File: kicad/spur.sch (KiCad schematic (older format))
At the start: 35 parts, among them J1 USB_A, SW1 JS102000SAQN, U1 MIC5377YC5, U2 AT25SF081-MAHB-X, U3 STM32F401CBUx, Y1 24MHz

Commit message: Remove UART test points
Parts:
- removed TP5: TXO, TestPoint:TestPoint_Pad_D1.0mm, symbol Connector:TestPoint
- removed TP6: RXI, TestPoint:TestPoint_Pad_D1.0mm, symbol Connector:TestPoint
- renumbered TP7 to TP5, TP8 to TP6
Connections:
- net UART_RXI: no longer names the net of U3.13 (PA3)
- net UART_TXO: no longer names the net of U3.12 (PA2)
- no-connect marks 23 -> 25
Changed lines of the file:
@@
 Sheet 1 1
 Title "Spur - A physical UEFI boot switch"
-Date "2020-09-20"
+Date "2020-09-22"
 Rev "v1.0"
 Comp "Ian Glen <ian@ianglen.me>"
@@
 	1    0    0    -1
 $EndComp
-Text Label 9800 4700 2    50   ~ 0
-UART_TXO
-Text Label 9800 4800 2    50   ~ 0
-UART_RXI
 Text Label 9800 5000 2    50   ~ 0
 SPI_SCK
@@
 Connection ~ 7000 3400
 $Comp
-L Connector:TestPoint TP7
+L Connector:TestPoint TP5
 U 1 1 5F6B941A
 P 9850 5800
-F 0 "TP7" V 9850 6050 50  0000 C CNN
+F 0 "TP5" V 9850 6050 50  0000 C CNN
 F 1 "SWDIO" V 9954 5872 50  0001 C CNN
 F 2 "TestPoint:TestPoint_Pad_D1.0mm" H 10050 5800 50  0001 C CNN
@@
 $EndComp
 $Comp
-L Connector:TestPoint TP8
+L Connector:TestPoint TP6
 U 1 1 5F6B9F42
 P 9850 5900
-F 0 "TP8" V 9850 6150 50  0000 C CNN
+F 0 "TP6" V 9850 6150 50  0000 C CNN
 F 1 "SWCLK" V 9954 5972 50  0001 C CNN
 F 2 "TestPoint:TestPoint_Pad_D1.0mm" H 10050 5900 50  0001 C CNN
@@
 Wire Wire Line
 	9350 5900 9850 5900
-$Comp
-L Connector:TestPoint TP5
-U 1 1 5F6C581E
-P 9850 4700
-F 0 "TP5" V 9850 4950 50  0000 C CNN
-F 1 "TXO" V 9954 4772 50  0001 C CNN
-F 2 "TestPoint:TestPoint_Pad_D1.0mm" H 10050 4700 50  0001 C CNN
-F 3 "~" H 10050 4700 50  0001 C CNN
-	1    9850 4700
-	0    1    1    0
-$EndComp
-$Comp
-L Connector:TestPoint TP6
-U 1 1 5F6C5828
-P 9850 4800
-F 0 "TP6" V 9850 5050 50  0000 C CNN
-F 1 "RXI" V 9954 4872 50  0001 C CNN
-F 2 "TestPoint:TestPoint_Pad_D1.0mm" H 10050 4800 50  0001 C CNN
-F 3 "~" H 10050 4800 50  0001 C CNN
-	1    9850 4800
-	0    1    1    0
-$EndComp
-Wire Wire Line
-	9350 4700 9850 4700
-Wire Wire Line
-	9350 4800 9850 4800
 $Comp
 L Connector:TestPoint TP2
@@
 Wire Wire Line
 	7500 4700 8050 4700
+NoConn ~ 9350 4700
+NoConn ~ 9350 4800
 $EndSCHEMATC

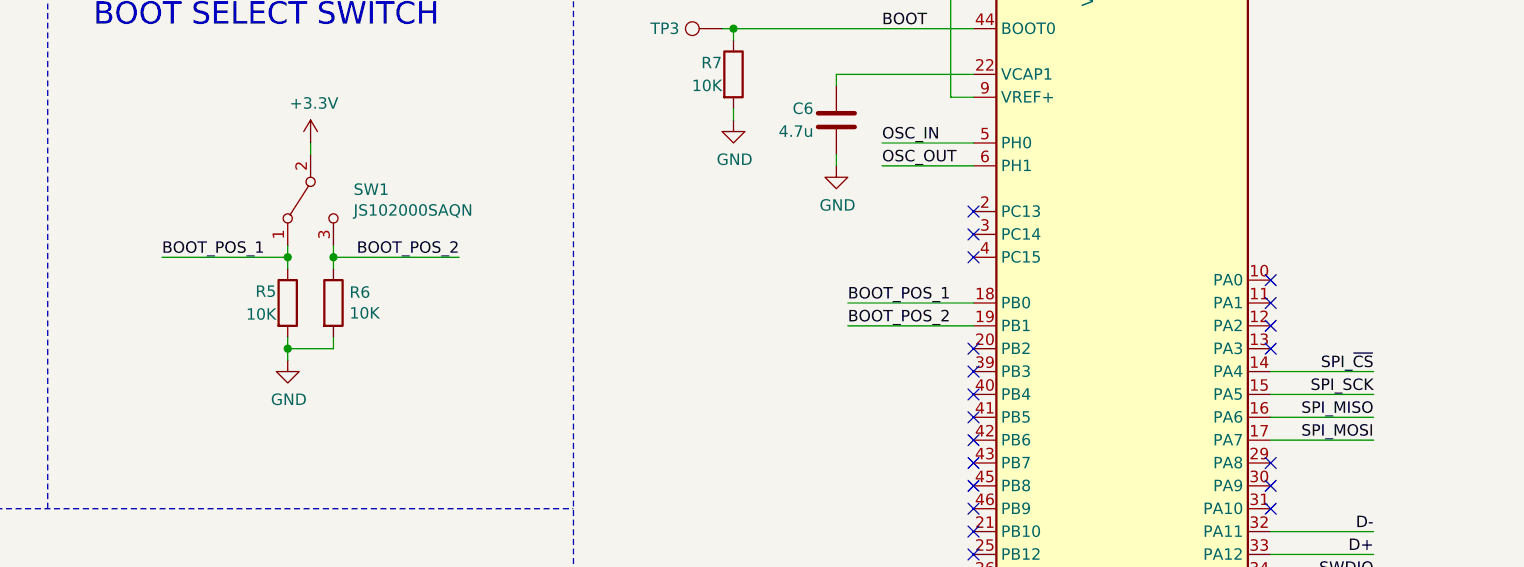
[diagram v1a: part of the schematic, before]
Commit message: Move switch input pins
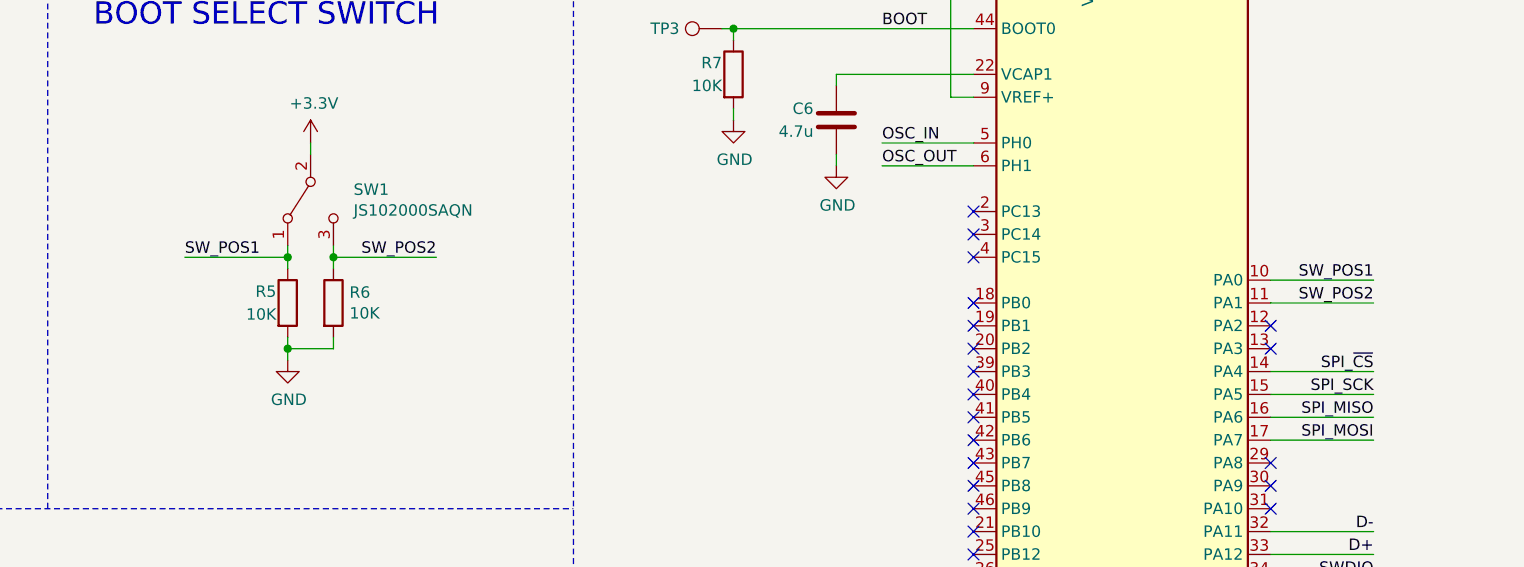
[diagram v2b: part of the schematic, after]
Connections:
- net SW_POS1: now reaches U3.10 (PA0)
- net SW_POS1: now also R5.1, SW1.1 (A)
- net SW_POS2: now reaches U3.11 (PA1)
- net SW_POS2: now also R6.1, SW1.3 (C)
- removed net BOOT_POS_1: R5.1, SW1.1 (A), U3.18 (PB0)
- removed net BOOT_POS_2: R6.1, SW1.3 (C), U3.19 (PB1)
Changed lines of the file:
@@
 Wire Wire Line
 	5050 4800 5050 4750
-Text Label 4500 4400 0    50   ~ 0
-BOOT_POS_1
-Text Label 5800 4400 2    50   ~ 0
-BOOT_POS_2
-Wire Wire Line
-	5800 4400 5250 4400
+Wire Wire Line
+	5700 4400 5250 4400
 Connection ~ 5250 4400
 Wire Wire Line
 	5250 4400 5250 4350
 Wire Wire Line
-	5050 4400 4500 4400
+	5050 4400 4600 4400
 Connection ~ 5050 4400
 Wire Wire Line
@@
 NoConn ~ 9350 5400
 NoConn ~ 9350 5300
-NoConn ~ 9350 4600
-NoConn ~ 9350 4500
 NoConn ~ 8050 6000
 NoConn ~ 8050 5900
@@
 Wire Wire Line
 	3200 4000 3150 4000
-Text Label 7500 4600 0    50   ~ 0
-BOOT_POS_1
-Text Label 7500 4700 0    50   ~ 0
-BOOT_POS_2
-Wire Wire Line
-	8050 4600 7500 4600
-Wire Wire Line
-	7500 4700 8050 4700
+Text Label 9800 4600 2    50   ~ 0
+SW_POS2
+Text Label 9800 4500 2    50   ~ 0
+SW_POS1
+Wire Wire Line
+	9350 4600 9800 4600
+Wire Wire Line
+	9800 4500 9350 4500
 NoConn ~ 9350 4700
 NoConn ~ 9350 4800
+NoConn ~ 8050 4700
+NoConn ~ 8050 4600
+Text Label 4600 4400 0    50   ~ 0
+SW_POS1
+Text Label 5700 4400 2    50   ~ 0
+SW_POS2
 $EndSCHEMATC

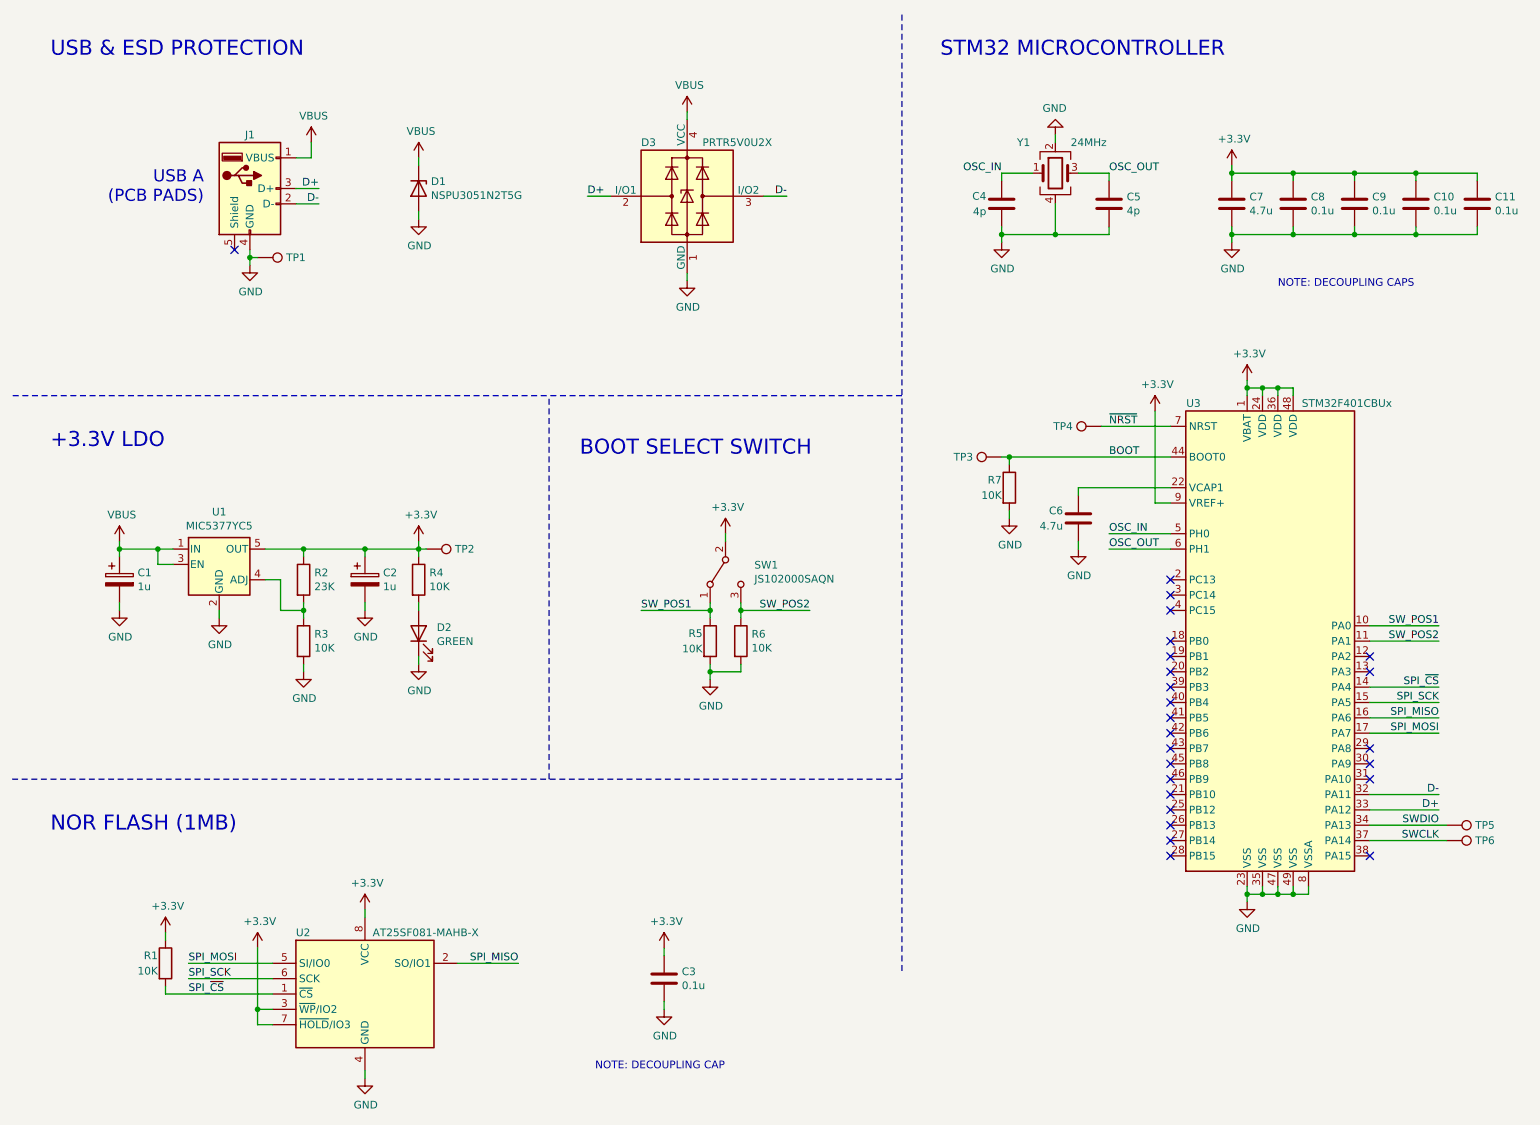
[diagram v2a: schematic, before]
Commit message: Update R2 value, fix C1 & C2 symbols, improve schematic notes
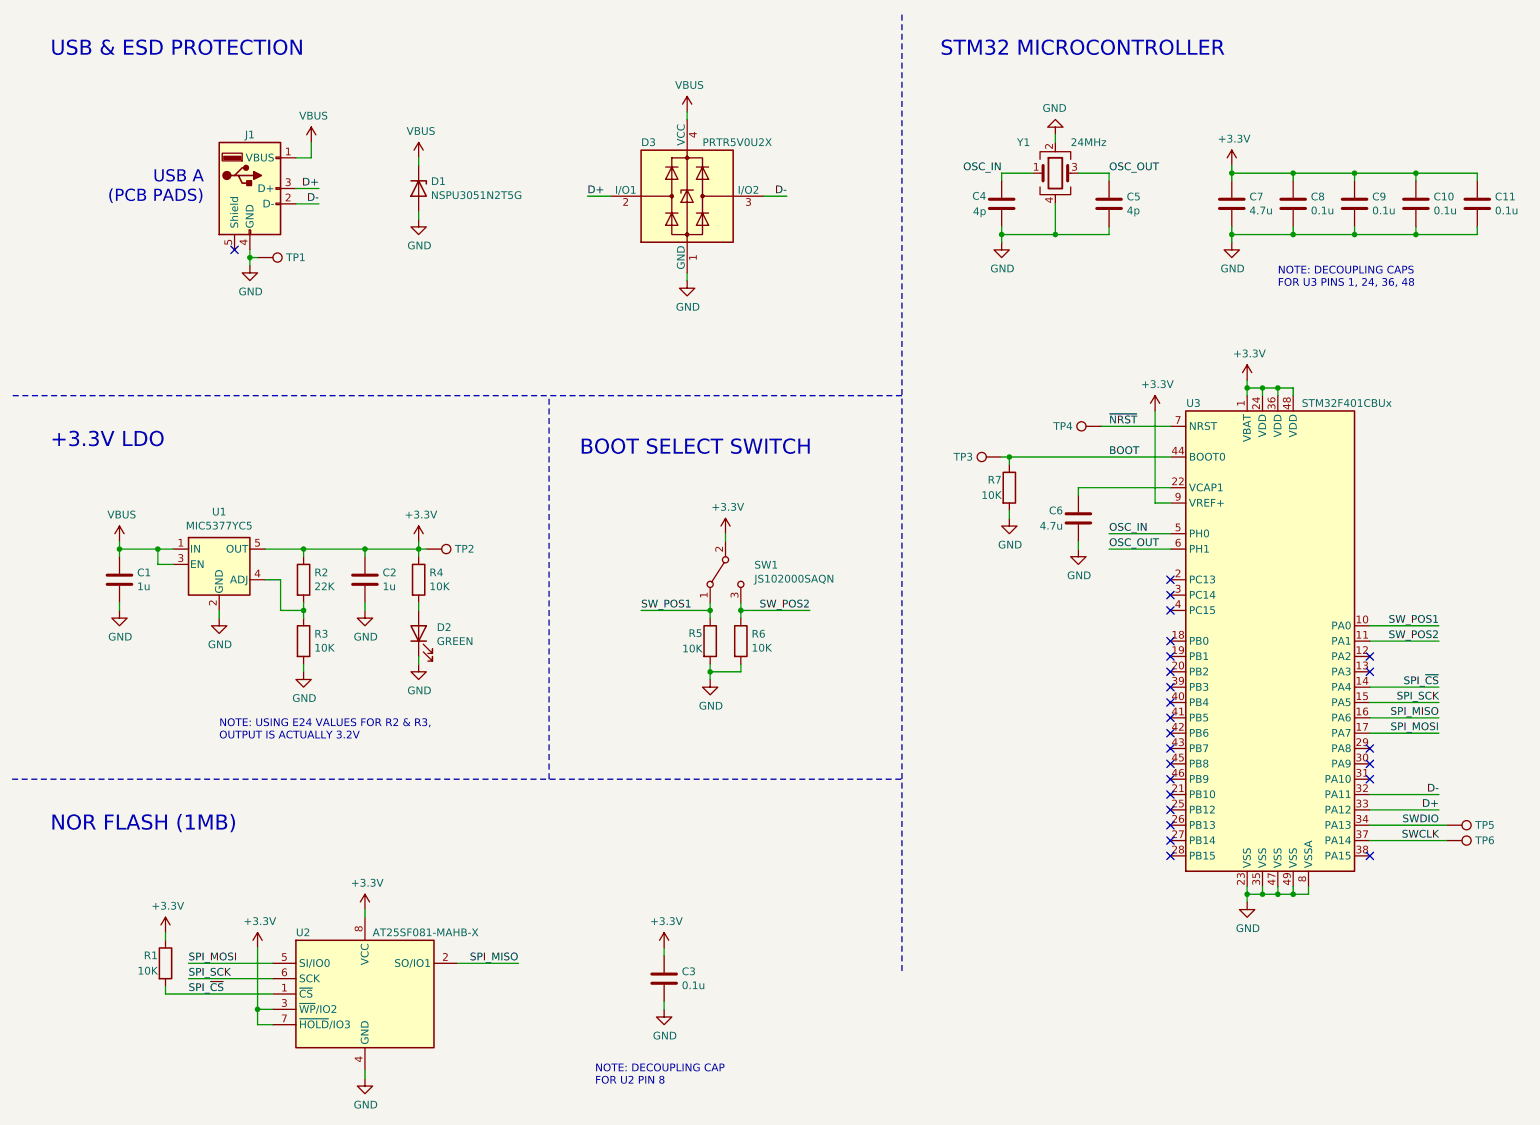
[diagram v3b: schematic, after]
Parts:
- removed C1, C2: 1u, Capacitor_SMD:C_0402_1005Metric, symbol Device:CP
- added C1, C2: 1u, Capacitor_SMD:C_0402_1005Metric, symbol Device:C
- R2: value 23K -> 22K
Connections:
- net +3V3: now also C2.1
- net GND: now also C1.2, C2.2
- net VBUS: now also C1.1
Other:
- note added: "NOTE: DECOUPLING CAPS\nFOR U3 PINS 1, 24, 36, 48"
- note added: "NOTE: DECOUPLING CAP\nFOR U2 PIN 8"
- note added: "NOTE: USING E24 VALUES FOR R2 & R3,\nOUTPUT IS ACTUALLY 3.2V"
- note removed: "NOTE: DECOUPLING CAP"
- note removed: "NOTE: DECOUPLING CAPS"
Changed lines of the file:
@@
 Sheet 1 1
 Title "Spur - A physical UEFI boot switch"
-Date "2020-09-22"
+Date "2020-09-25"
 Rev "v1.0"
 Comp "Ian Glen <ian@ianglen.me>"
@@
 	500  5500 6300 5500
 $Comp
-L Device:CP C1
-U 1 1 5F69995A
-P 1200 4200
-F 0 "C1" H 1318 4246 50  0000 L CNN
-F 1 "1u" H 1318 4155 50  0000 L CNN
-F 2 "Capacitor_SMD:C_0402_1005Metric" H 1238 4050 50  0001 C CNN
-F 3 "~" H 1200 4200 50  0001 C CNN
-	1    1200 4200
-	1    0    0    -1
-$EndComp
-$Comp
 L power:GND #PWR0111
 U 1 1 5F69A270
@@
 	1550 4000 1450 4000
 $Comp
-L Device:CP C2
-U 1 1 5F69D2F8
-P 2800 4200
-F 0 "C2" H 2918 4246 50  0000 L CNN
-F 1 "1u" H 2918 4155 50  0000 L CNN
-F 2 "Capacitor_SMD:C_0402_1005Metric" H 2838 4050 50  0001 C CNN
-F 3 "~" H 2800 4200 50  0001 C CNN
-	1    2800 4200
-	1    0    0    -1
-$EndComp
-$Comp
 L power:GND #PWR0112
 U 1 1 5F69D302
@@
 P 2400 4200
 F 0 "R2" H 2470 4246 50  0000 L CNN
-F 1 "23K" H 2470 4155 50  0000 L CNN
+F 1 "22K" H 2470 4155 50  0000 L CNN
 F 2 "Resistor_SMD:R_0402_1005Metric" V 2330 4200 50  0001 C CNN
 F 3 "~" H 2400 4200 50  0001 C CNN
@@
 Text Label 7650 3200 0    50   ~ 0
 ~NRST
-Text Notes 4300 7400 0    50   ~ 0
-NOTE: DECOUPLING CAP
+Text Notes 4300 7500 0    50   ~ 0
+NOTE: DECOUPLING CAP\nFOR U2 PIN 8
 Wire Wire Line
 	7950 3100 7950 3700
@@
 	9800 4900 9350 4900
 Text Notes 8750 2300 0    50   ~ 0
-NOTE: DECOUPLING CAPS
+NOTE: DECOUPLING CAPS\nFOR U3 PINS 1, 24, 36, 48
 $Comp
 L power:+3.3V #PWR0130
@@
 Text Label 5700 4400 2    50   ~ 0
 SW_POS2
+Text Notes 1850 5250 0    50   ~ 0
+NOTE: USING E24 VALUES FOR R2 & R3,\nOUTPUT IS ACTUALLY 3.2V
+$Comp
+L Device:C C1
+U 1 1 5F6F755F
+P 1200 4200
+F 0 "C1" H 1315 4246 50  0000 L CNN
+F 1 "1u" H 1315 4155 50  0000 L CNN
+F 2 "Capacitor_SMD:C_0402_1005Metric" H 1238 4050 50  0001 C CNN
+F 3 "~" H 1200 4200 50  0001 C CNN
+	1    1200 4200
+	1    0    0    -1
+$EndComp
+$Comp
+L Device:C C2
+U 1 1 5F6F9410
+P 2800 4200
+F 0 "C2" H 2915 4246 50  0000 L CNN
+F 1 "1u" H 2915 4155 50  0000 L CNN
+F 2 "Capacitor_SMD:C_0402_1005Metric" H 2838 4050 50  0001 C CNN
+F 3 "~" H 2800 4200 50  0001 C CNN
+	1    2800 4200
+	1    0    0    -1
+$EndComp
 $EndSCHEMATC

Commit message: Switch to internal pull-ups, remove 4.7uF bulk cap
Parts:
- removed C7: 4.7u, Capacitor_SMD:C_0402_1005Metric, symbol Device:C
- removed D2: GREEN, LED_SMD:LED_0402_1005Metric, symbol Device:LED
- removed R1, R4, R5, R6: 10K, Resistor_SMD:R_0402_1005Metric, symbol Device:R
- renumbered C11 to C10, C8 to C7, C9 to C8, C10 to C9, D3 to D2, R2 to R1, R3 to R2, R7 to R3
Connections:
- net +3V3: no longer SW1.2 (B)
- net GND: now also SW1.2 (B)
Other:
- note added: "NOTE: ENABLE INTERNAL PULL-UPS\nON SW_POS1, SW_POS2, AND SPI_~CS"
- moved on the sheet: C1, C10, C2, C7, C8, C9, R1, R2, SW1, TP2, U1

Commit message: Add custom footprint for flash chip
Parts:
- U2: footprint Package_SON:SON-8-1EP_3x2mm_P0.5mm_EP1.4x1.6mm -> spur:SON-8-1EP_3x2mm_P0.5mm_EP0.2x1.6mm
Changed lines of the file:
@@
 F 0 "U2" H 2350 7300 50  0000 L CNN
 F 1 "AT25SF081-MAHB-X" H 2850 7300 50  0000 L CNN
-F 2 "Package_SON:SON-8-1EP_3x2mm_P0.5mm_EP1.4x1.6mm" H 2800 6300 50  0001 C CNN
+F 2 "spur:SON-8-1EP_3x2mm_P0.5mm_EP0.2x1.6mm" H 2800 6300 50  0001 C CNN
 F 3 "https://www.adestotech.com/wp-content/uploads/DS-AT25SF081_045.pdf" H 2800 6900 50  0001 C CNN
 	1    2800 6900

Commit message: Add PCB layout
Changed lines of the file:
@@
 $EndDescr
-$Comp
-L Connector:USB_A J1
-U 1 1 5F640CFE
-P 2050 1650
-F 0 "J1" H 2050 2000 50  0000 C CNN
-F 1 "USB_A" H 2107 2026 50  0001 C CNN
-F 2 "spur:USB_A_pads" H 2200 1600 50  0001 C CNN
-F 3 " ~" H 2200 1600 50  0001 C CNN
-	1    2050 1650
-	1    0    0    -1
-$EndComp
 $Comp
 L spur:AT25SF081-MAHB-X U2
@@
 Wire Wire Line
 	1650 6900 2200 6900
+$Comp
+L Connector:USB_A J1
+U 1 1 5FC9E106
+P 2050 1650
+F 0 "J1" H 2050 2000 50  0000 C CNN
+F 1 "USB_A" H 2107 2026 50  0001 C CNN
+F 2 "spur:USB_A_pads" H 2200 1600 50  0001 C CNN
+F 3 " ~" H 2200 1600 50  0001 C CNN
+	1    2050 1650
+	1    0    0    -1
+$EndComp
+Connection ~ 3150 1850
 $EndSCHEMATC
